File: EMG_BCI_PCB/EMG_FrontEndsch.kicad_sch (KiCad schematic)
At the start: 28 parts, among them U1 INA350CDS, U2 ADA4807-4ARUZ

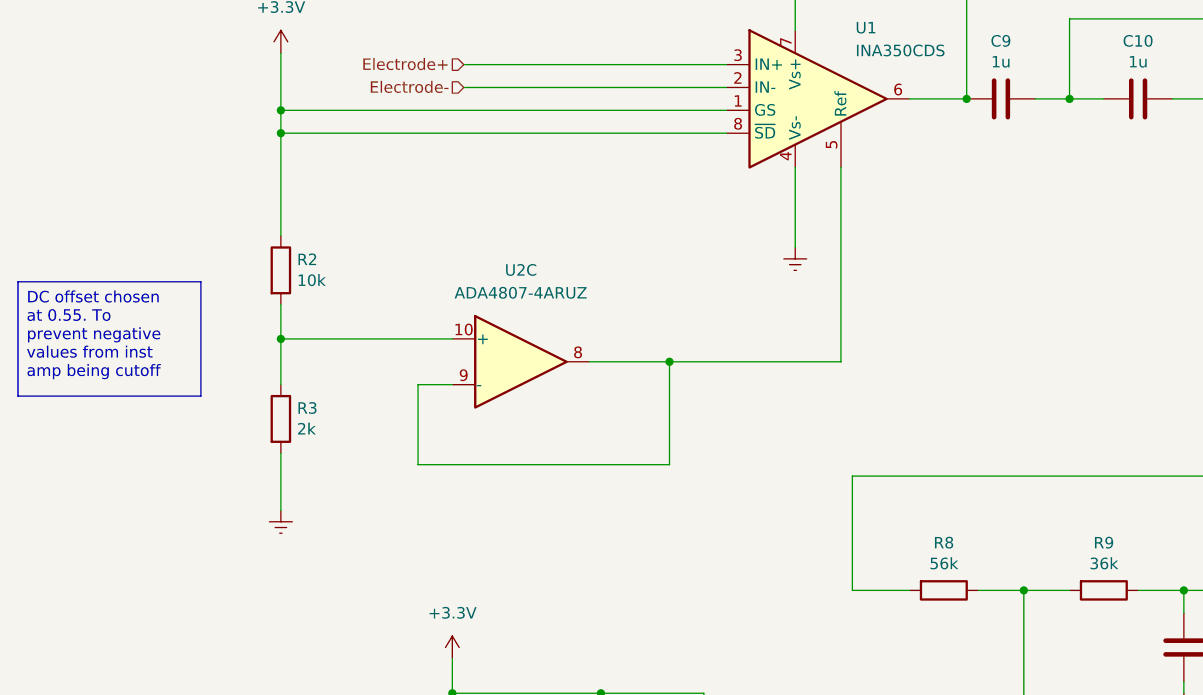
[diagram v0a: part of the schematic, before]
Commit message: Add the negative voltage supply to the instrumentation amplifier
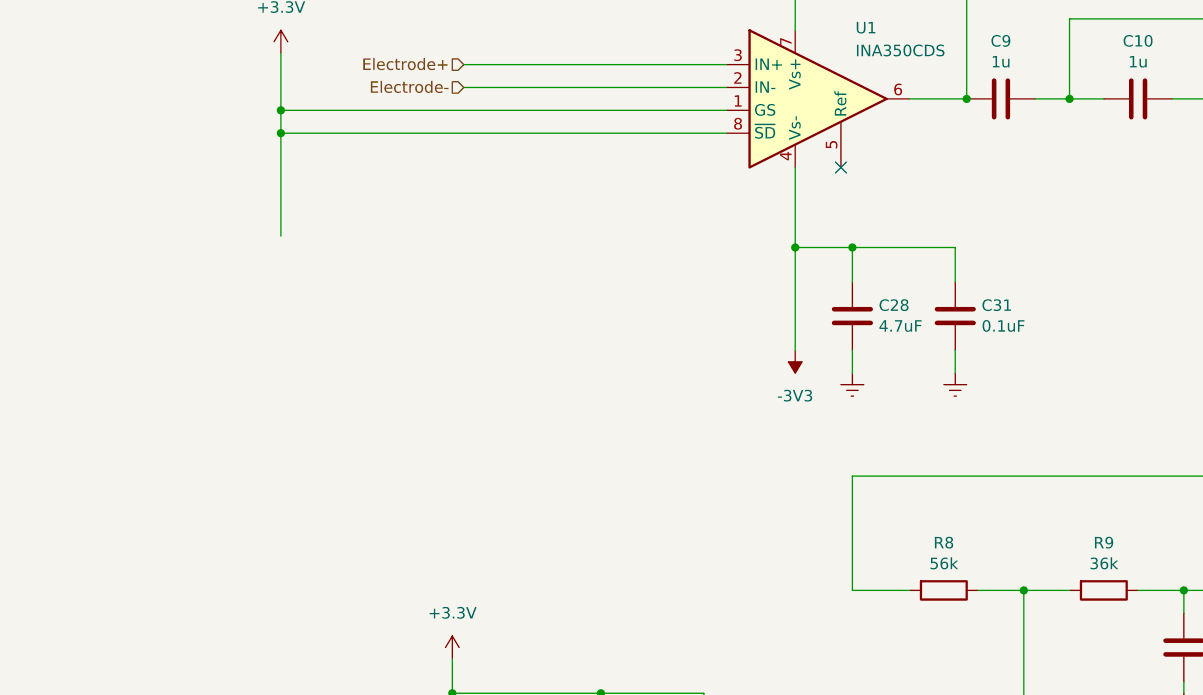
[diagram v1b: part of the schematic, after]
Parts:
- removed R2: 10k, Resistor_SMD:R_0603_1608Metric_Pad0.98x0.95mm_HandSolder, symbol Device:R
- removed R3: 2k, Resistor_SMD:R_0603_1608Metric_Pad0.98x0.95mm_HandSolder, symbol Device:R
- removed unit 3 of U2
- added C28: 4.7uF, Capacitor_SMD:C_0603_1608Metric_Pad1.08x0.95mm_HandSolder, symbol Device:C
- added C31: 0.1uF, Capacitor_SMD:C_0603_1608Metric_Pad1.08x0.95mm_HandSolder, symbol Device:C
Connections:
- net -3V3: now also U1.4 (Vs-), C28.1, C31.1
- net Earth: now also C28.2, C31.2; no longer U1.4 (Vs-)
- no-connect marks 0 -> 1
